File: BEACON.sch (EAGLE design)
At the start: 21 parts, among them IC1 SPARKCORE, IC2 TX-C1FLAT, IC3 RXB1SHORTFLAT, T1 BPX81

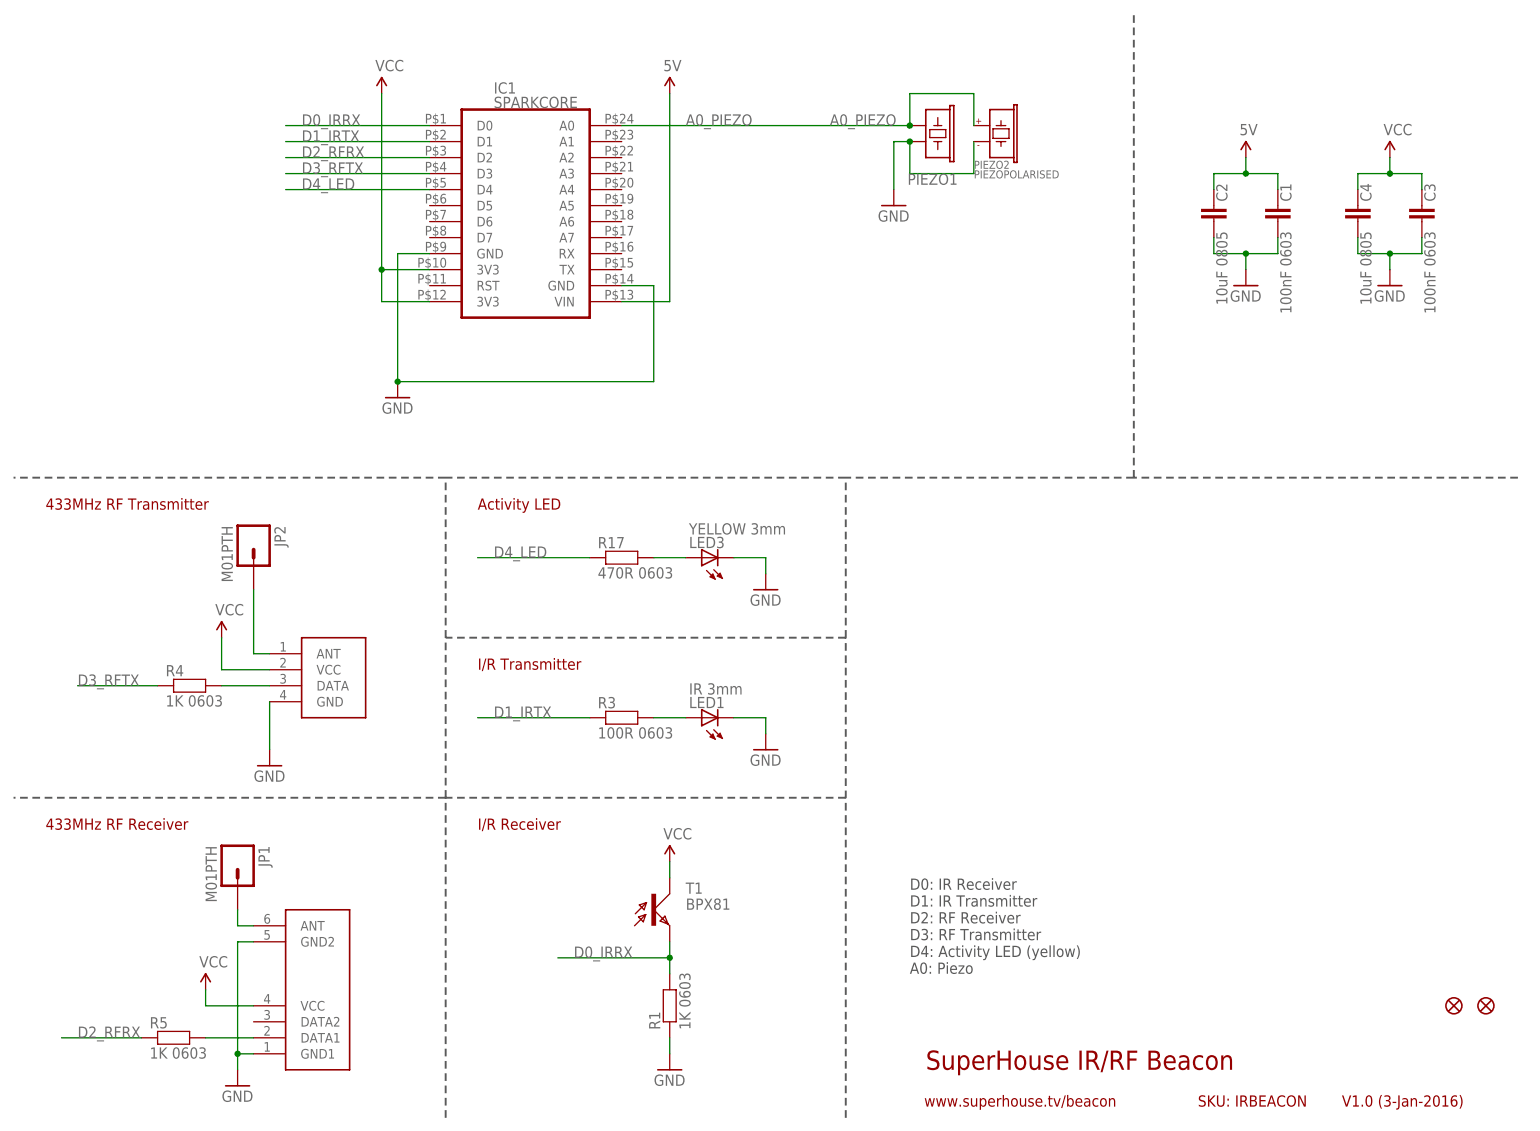
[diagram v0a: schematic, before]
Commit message: Reduced PCB outline and added action button to initiate binding
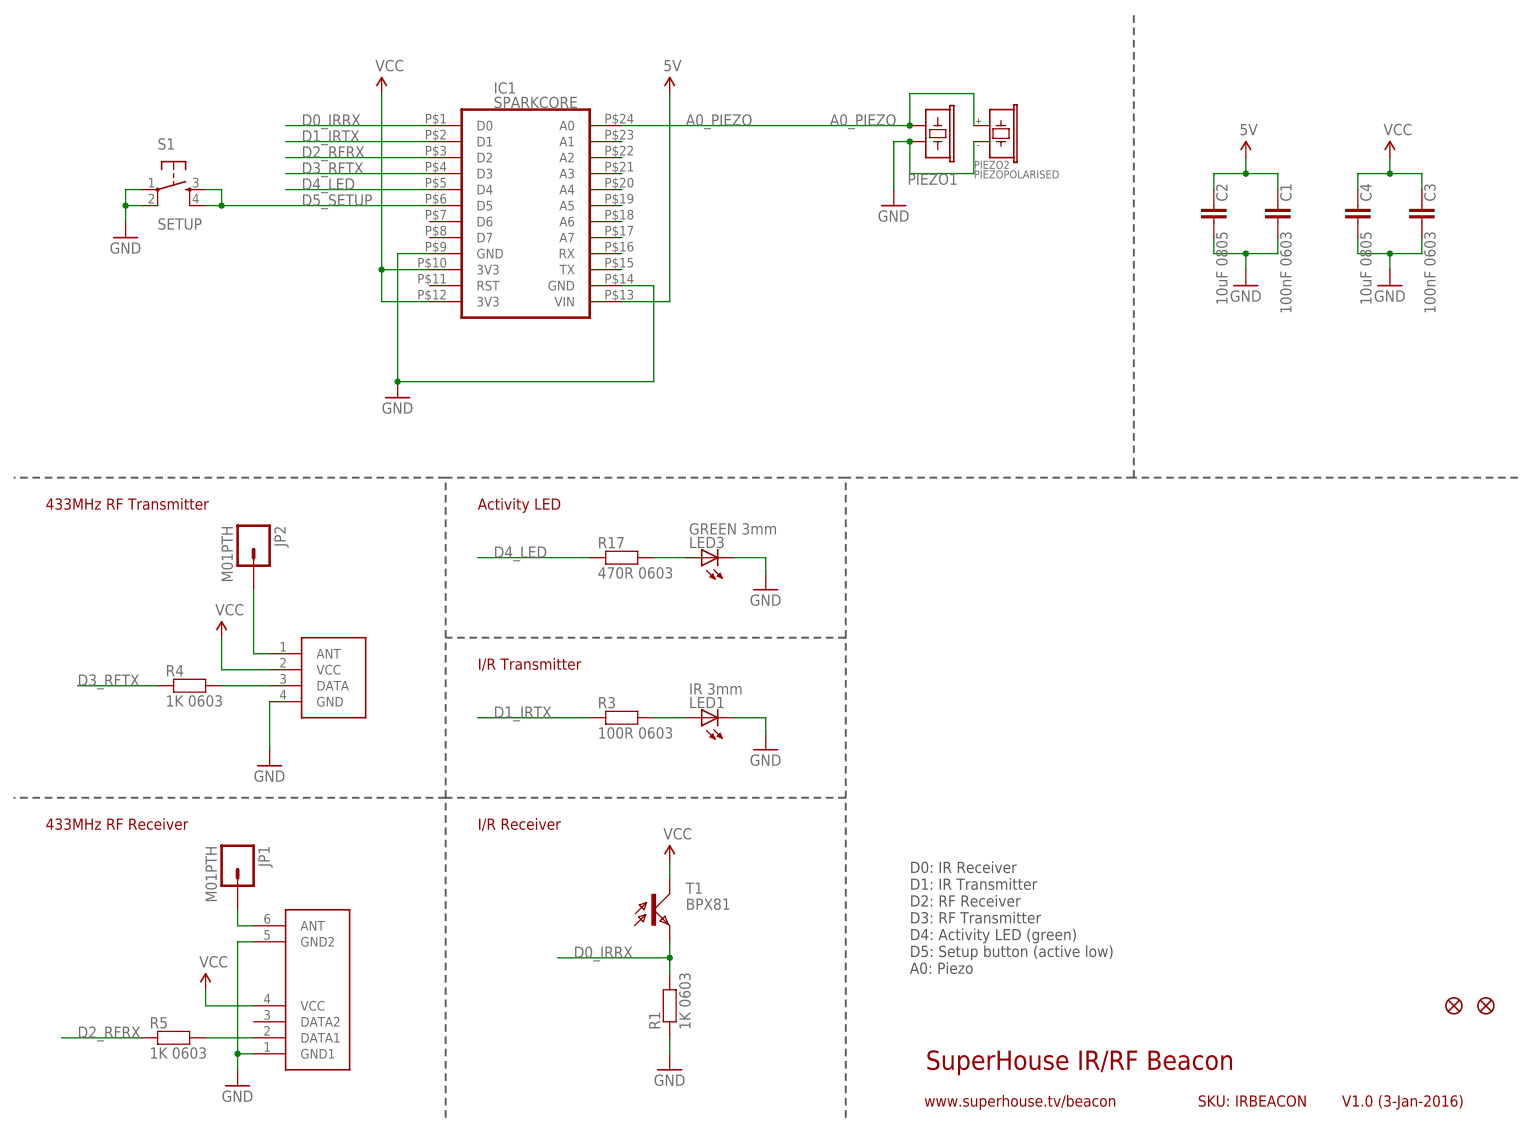
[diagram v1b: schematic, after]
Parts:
- added S1: SETUP, freetronics-original:TAC_SWITCHPTH
- LED3: value YELLOW 3mm -> GREEN 3mm
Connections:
- new net D5_SETUP: IC1.D5, S1.3, S1.4
- net GND: now also S1.1, S1.2
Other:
- note added: "D0: IR Receiver D1: IR Transmitter D2: RF Receiver D3: RF Transmitter D4: Activity LED (green) D5: Setup button (active low) A0: Piezo"
- note removed: "D0: IR Receiver D1: IR Transmitter D2: RF Receiver D3: RF Transmitter D4: Activity LED (yellow) A0: Piezo"
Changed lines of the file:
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@@
 <?xml version="1.0" encoding="utf-8"?>
 <!DOCTYPE eagle SYSTEM "eagle.dtd">
-<eagle version="6.5.0">
+<eagle version="9.0.1">
 <drawing>
 <settings>
 <setting alwaysvectorfont="yes"/>
+<setting keepoldvectorfont="yes"/>
 <setting verticaltext="up"/>
 </settings>
@@
 <layer number="2" name="Route2" color="1" fill="3" visible="no" active="no"/>
 <layer number="3" name="Route3" color="4" fill="3" visible="no" active="no"/>
+<layer number="4" name="Route4" color="1" fill="4" visible="no" active="no"/>
+<layer number="5" name="Route5" color="4" fill="4" visible="no" active="no"/>
+<layer number="6" name="Route6" color="1" fill="8" visible="no" active="no"/>
+<layer number="7" name="Route7" color="4" fill="8" visible="no" active="no"/>
+<layer number="8" name="Route8" color="1" fill="2" visible="no" active="no"/>
+<layer number="9" name="Route9" color="4" fill="2" visible="no" active="no"/>
+<layer number="10" name="Route10" color="1" fill="7" visible="no" active="no"/>
+<layer number="11" name="Route11" color="4" fill="7" visible="no" active="no"/>
+<layer number="12" name="Route12" color="1" fill="5" visible="no" active="no"/>
+<layer number="13" name="Route13" color="4" fill="5" visible="no" active="no"/>
 <layer number="14" name="Route14" color="1" fill="6" visible="no" active="no"/>
 <layer number="15" name="Route15" color="4" fill="6" visible="no" active="no"/>
@@
 <part name="U$5" library="freetronics-original" deviceset="FIDUCIAL" device="1X2.5"/>
 <part name="C2" library="freetronics-jon" deviceset="C-EU" device="C0805" value="10uF 0805"/>
-<part name="LED3" library="freetronics-2" deviceset="LED" device="3MM" value="YELLOW 3mm"/>
+<part name="LED3" library="freetronics-2" deviceset="LED" device="3MM" value="GREEN 3mm"/>
 <part name="R17" library="freetronics-jon" deviceset="RESISTOR" device="0603" value="470R 0603"/>
 <part name="IC1" library="freetronics-jon" deviceset="SPARKCORE" device=""/>
@@
 <part name="C4" library="freetronics-jon" deviceset="C-EU" device="C0805" value="10uF 0805"/>
 <part name="GND2" library="freetronics" deviceset="GND" device=""/>
+<part name="S1" library="freetronics-original" deviceset="TAC_SWITCH" device="PTH" value="SETUP"/>
+<part name="GND3" library="freetronics" deviceset="GND" device=""/>
 </parts>
 <sheets>
@@
 D2: RF Receiver
 D3: RF Transmitter
-D4: Activity LED (yellow)
+D4: Activity LED (green)
+D5: Setup button (active low)
 A0: Piezo</text>
 <text x="10.16" y="101.6" size="1.778" layer="94">433MHz RF Transmitter</text>
@@
 </instance>
 <instance part="GND2" gate="1" x="223.52" y="137.16"/>
+<instance part="S1" gate="S" x="30.48" y="152.4"/>
+<instance part="GND3" gate="1" x="22.86" y="144.78"/>
 </instances>
 <busses>
@@
 <wire x1="228.6" y1="142.24" x2="223.52" y2="142.24" width="0.1524" layer="91"/>
 <junction x="223.52" y="142.24"/>
+</segment>
+<segment>
+<pinref part="S1" gate="S" pin="2"/>
+<pinref part="GND3" gate="1" pin="GND"/>
+<wire x1="25.4" y1="149.86" x2="22.86" y2="149.86" width="0.1524" layer="91"/>
+<wire x1="22.86" y1="149.86" x2="22.86" y2="147.32" width="0.1524" layer="91"/>
+<pinref part="S1" gate="S" pin="1"/>
+<wire x1="25.4" y1="152.4" x2="22.86" y2="152.4" width="0.1524" layer="91"/>
+<wire x1="22.86" y1="152.4" x2="22.86" y2="149.86" width="0.1524" layer="91"/>
+<junction x="22.86" y="149.86"/>
 </segment>
 </net>
@@
 </segment>
 </net>
+<net name="D5_SETUP" class="0">
+<segment>
+<pinref part="S1" gate="S" pin="3"/>
+<wire x1="35.56" y1="152.4" x2="38.1" y2="152.4" width="0.1524" layer="91"/>
+<wire x1="38.1" y1="152.4" x2="38.1" y2="149.86" width="0.1524" layer="91"/>
+<pinref part="S1" gate="S" pin="4"/>
+<wire x1="38.1" y1="149.86" x2="35.56" y2="149.86" width="0.1524" layer="91"/>
+<pinref part="IC1" gate="G$1" pin="D5"/>
+<wire x1="38.1" y1="149.86" x2="71.12" y2="149.86" width="0.1524" layer="91"/>
+<junction x="38.1" y="149.86"/>
+<label x="50.8" y="149.86" size="1.778" layer="95"/>
+</segment>
+</net>

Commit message: Added mechanical details
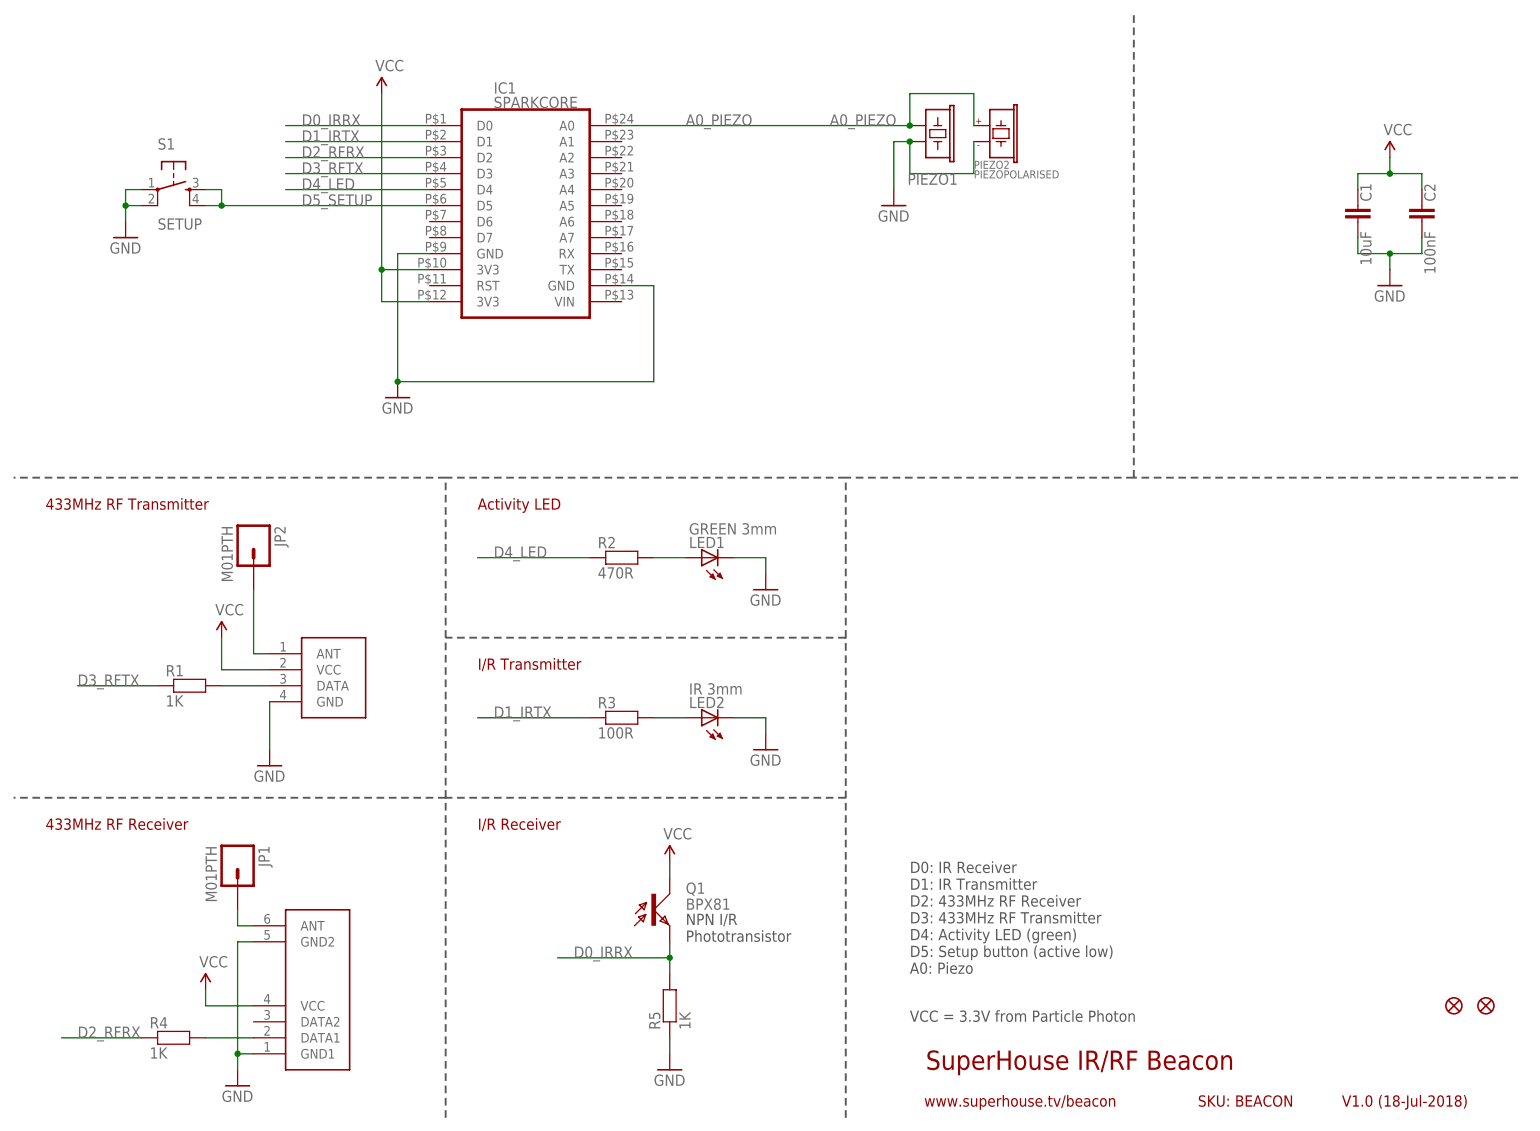
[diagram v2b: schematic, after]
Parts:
- removed C3: 100nF 0603, freetronics:CAP0603
- removed C4: 10uF 0805, freetronics-jon:C-EUC0805
- removed LED3: GREEN 3mm, freetronics-2:LED3MM
- added LED2: IR 3mm, freetronics-2:LED3MM
- C1: value 100nF 0603 -> 10uF; device freetronics:CAP0603 -> freetronics-jon:C-EUC0805
- C2: value 10uF 0805 -> 100nF; device freetronics-jon:C-EUC0805 -> freetronics:CAP0603
- LED1: value IR 3mm -> GREEN 3mm
- R1, R4, R5: value 1K 0603 -> 1K
- R2: value 470R 0603 -> 470R
- R3: value 100R 0603 -> 100R
- renumbered R17 to R2, T1 to Q1
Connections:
- removed net 5V: C1.1, C2.2, IC1.VIN
- net D0_IRRX: now also R5.2; no longer R1.2
- net D2_RFRX: now also R4.1; no longer R5.1
- net D3_RFTX: now also R1.1; no longer R4.1
- net GND: now also C1.1, C2.2, LED2.C, R5.1; no longer C1.2, C2.1, C3.2, C4.1, LED3.C, R1.1
- net N$1: now also LED1.A; no longer LED3.A
- net N$13: now also R4.2; no longer R5.2
- net N$2: now also R1.2; no longer R4.2
- net N$3: now also LED2.A; no longer LED1.A
- net VCC: now also C1.2, C2.1; no longer C3.1, C4.2
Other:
- note added: "D0: IR Receiver D1: IR Transmitter D2: 433MHz RF Receiver D3: 433MHz RF Transmitter D4: Activity LED (green) D5: Setup button (active low) A0: Piezo"
- note added: "NPN I/R Phototransistor"
- note added: "SKU: BEACON"
- note added: "V1.0 (18-Jul-2018)"
- note added: "VCC = 3.3V from Particle Photon"
- note removed: "D0: IR Receiver D1: IR Transmitter D2: RF Receiver D3: RF Transmitter D4: Activity LED (green) D5: Setup button (active low) A0: Piezo"
- note removed: "SKU: IRBEACON"
- note removed: "V1.0 (3-Jan-2016)"
- moved on the sheet: C1, C2, LED1, R1, R4, R5
